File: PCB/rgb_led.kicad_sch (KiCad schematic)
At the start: 3 parts

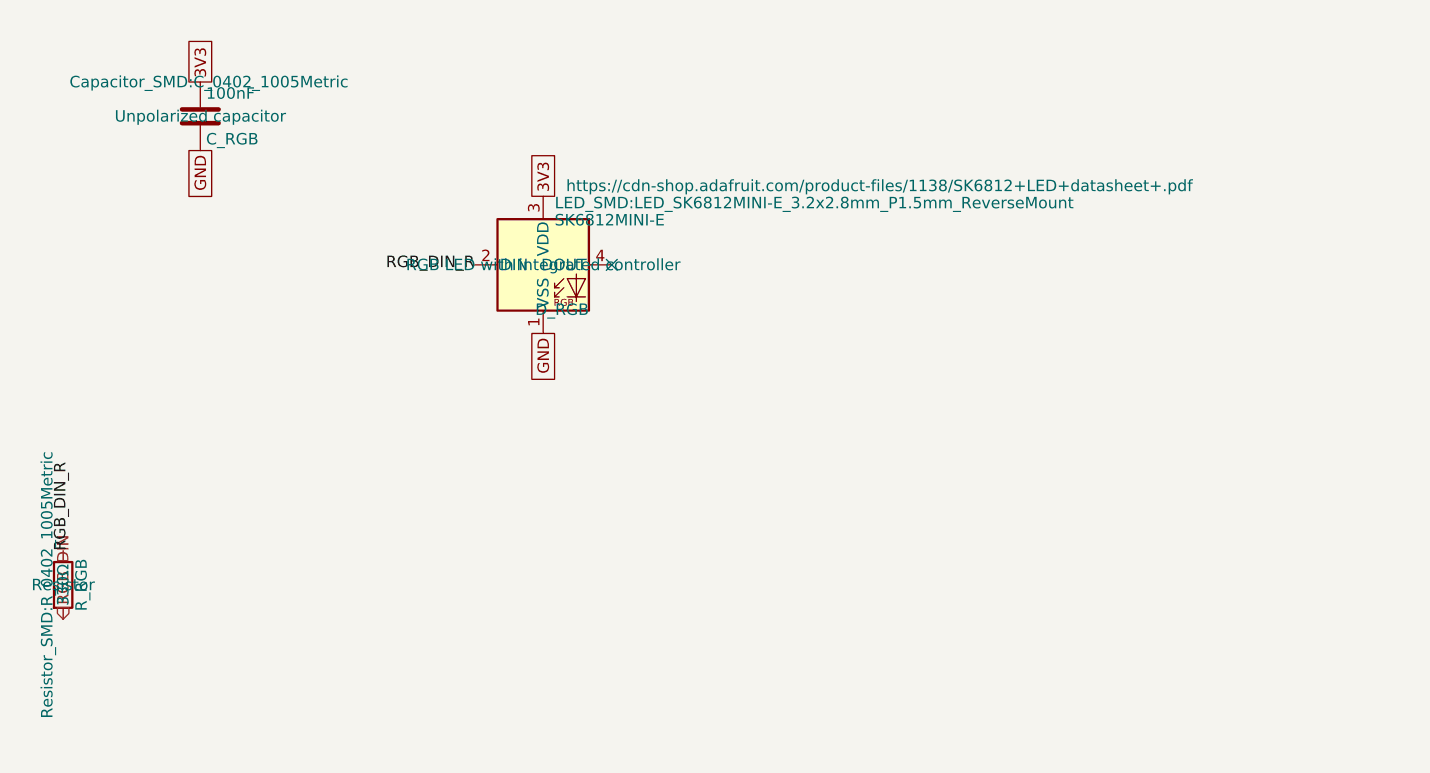
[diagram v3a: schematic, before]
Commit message: layout: everything is on the board
The board edge cuts are down to 100mm x 35mm. All the components have the right footprints and are on the board, but no traces exist yet, and not all circuits are laid out properly yet. Lots of DRC warnings.
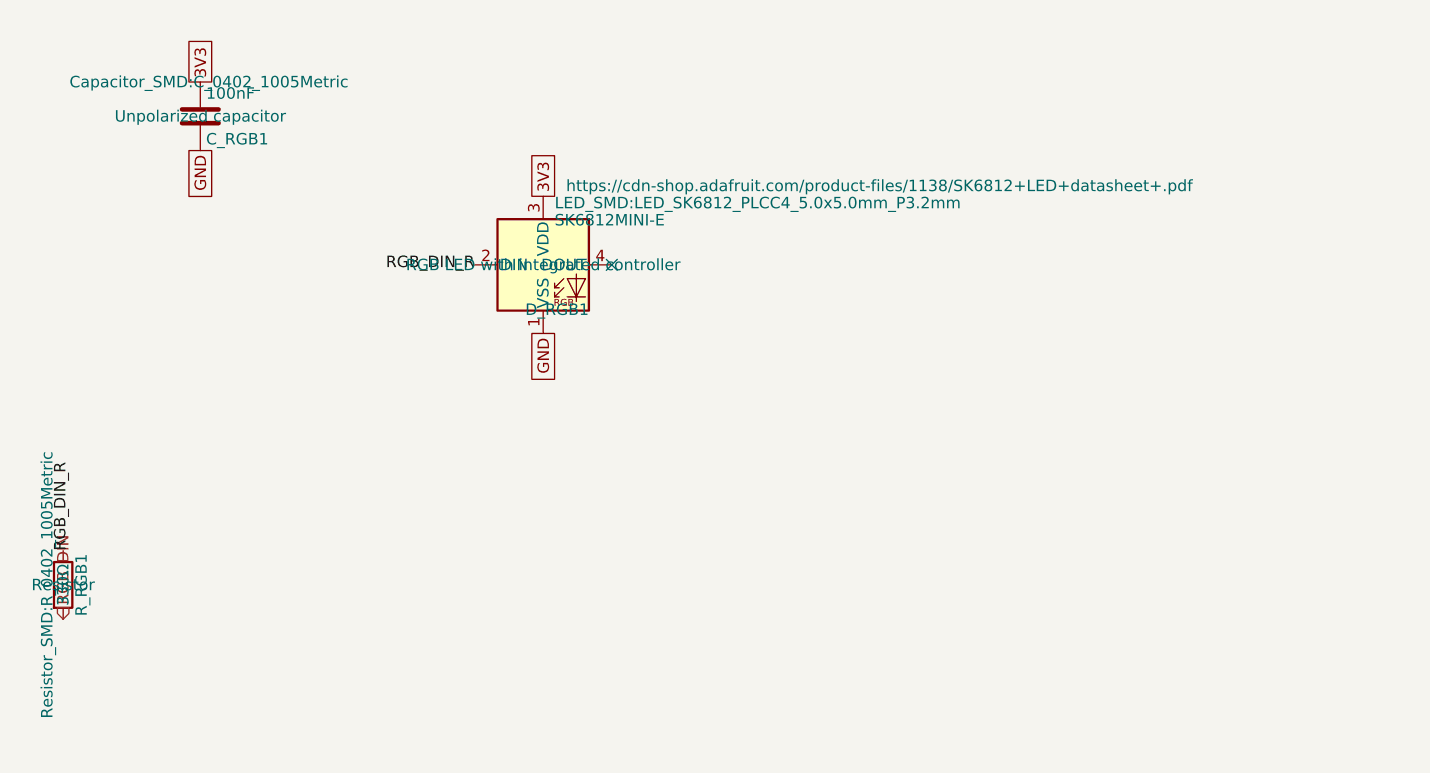
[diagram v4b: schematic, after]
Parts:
- removed C_RGB: 100nF, Capacitor_SMD:C_0402_1005Metric, symbol Device:C
- removed D_RGB: SK6812MINI-E, LED_SMD:LED_SK6812MINI-E_3.2x2.8mm_P1.5mm_ReverseMount, symbol LED:SK6812
- removed R_RGB: 330Ω, Resistor_SMD:R_0402_1005Metric, symbol Device:R
- added C_RGB1: 100nF, Capacitor_SMD:C_0402_1005Metric, symbol Device:C
- added D_RGB1: SK6812MINI-E, LED_SMD:LED_SK6812_PLCC4_5.0x5.0mm_P3.2mm, symbol LED:SK6812
- added R_RGB1: 330Ω, Resistor_SMD:R_0402_1005Metric, symbol Device:R
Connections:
- net 3V3: now also C_RGB1.1, D_RGB1.3 (VDD)
- net GND: now also C_RGB1.2, D_RGB1.1 (VSS)
- net RGB_DIN: now also R_RGB1.2
- net RGB_DIN_R: now also D_RGB1.2 (DIN), R_RGB1.1
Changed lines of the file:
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@@
+		)
+	)
+	(global_label "GND"
+		(shape passive)
+		(at 175.26 102.87 270)
+		(fields_autoplaced yes)
+		(effects
+			(font
+				(size 1.27 1.27)
+			)
+			(justify right)
+		)
+		(property "Intersheetrefs" "${INTERSHEET_REFS}"
+			(at 175.26 102.87 0)
+			(hide yes)
+			(show_name no)
+			(do_not_autoplace no)
+			(effects
+				(font
+					(size 1.27 1.27)
+				)
+			)
+		)
+	)
+	(global_label "GND"
+		(shape passive)
+		(at 137.16 82.55 270)
+		(fields_autoplaced yes)
+		(effects
+			(font
+				(size 1.27 1.27)
+			)
+			(justify right)
+		)
+		(property "Intersheetrefs" "${INTERSHEET_REFS}"
+			(at 137.16 82.55 0)
+			(hide yes)
+			(show_name no)
+			(do_not_autoplace no)
+			(effects
+				(font
+					(size 1.27 1.27)
+				)
+			)
+		)
+	)
+	(global_label "3V3"
+		(shape passive)
+		(at 137.16 74.93 90)
+		(fields_autoplaced yes)
+		(effects
+			(font
+				(size 1.27 1.27)
+			)
+			(justify left)
+		)
+		(property "Intersheetrefs" "${INTERSHEET_REFS}"
+			(at 137.16 74.93 0)
+			(hide yes)
+			(show_name no)
+			(do_not_autoplace no)
+			(effects
+				(font
+					(size 1.27 1.27)
+				)
+			)
 		)
 	)
@@
 		(property "Intersheetrefs" "${INTERSHEET_REFS}"
 			(at 175.26 87.63 0)
-			(hide yes)
-			(show_name no)
-			(do_not_autoplace no)
-			(effects
-				(font
-					(size 1.27 1.27)
-				)
-			)
-		)
-	)
-	(global_label "GND"
-		(shape passive)
-		(at 175.26 102.87 270)
-		(fields_autoplaced yes)
-		(effects
-			(font
-				(size 1.27 1.27)
-			)
-			(justify right)
-		)
-		(property "Intersheetrefs" "${INTERSHEET_REFS}"
-			(at 175.26 102.87 0)
-			(hide yes)
-			(show_name no)
-			(do_not_autoplace no)
-			(effects
-				(font
-					(size 1.27 1.27)
-				)
-			)
-		)
-	)
-	(global_label "GND"
-		(shape passive)
-		(at 137.16 82.55 270)
-		(fields_autoplaced yes)
-		(effects
-			(font
-				(size 1.27 1.27)
-			)
-			(justify right)
-		)
-		(property "Intersheetrefs" "${INTERSHEET_REFS}"
-			(at 137.16 82.55 0)
-			(hide yes)
-			(show_name no)
-			(do_not_autoplace no)
-			(effects
-				(font
-					(size 1.27 1.27)
-				)
-			)
-		)
-	)
-	(global_label "3V3"
-		(shape passive)
-		(at 137.16 74.93 90)
-		(fields_autoplaced yes)
-		(effects
-			(font
-				(size 1.27 1.27)
-			)
-			(justify left)
-		)
-		(property "Intersheetrefs" "${INTERSHEET_REFS}"
-			(at 137.16 74.93 0)
 			(hide yes)
 			(show_name no)
@@
 		(dnp no)
 		(fields_autoplaced yes)
-		(property "Reference" "C_RGB"
+		(property "Reference" "C_RGB1"
 			(at 137.795 81.28 0)
 			(show_name no)
@@
 		(instances
 			(project "snips_controller"
-				(path "/f9d779c6-e1a6-4677-9004-6e9cc3d2fa8d/de2e61c0-3a94-4f0a-93aa-fbb224e49852"
-					(reference "C_RGB")
+				(path "/21935953-32a0-46ad-8079-8177920c6978/b63260e5-0a73-448f-8e04-69b17654f975"
+					(reference "C_RGB1")
+					(unit 1)
+				)
+			)
+		)
+	)
+	(symbol
+		(lib_id "Device:R")
+		(at 121.92 130.81 0)
+		(unit 1)
+		(body_style 1)
+		(exclude_from_sim no)
+		(in_bom yes)
+		(on_board yes)
+		(in_pos_files yes)
+		(dnp no)
+		(fields_autoplaced yes)
+		(property "Reference" "R_RGB1"
+			(at 123.952 130.81 90)
+			(show_name no)
+			(do_not_autoplace no)
+			(effects
+				(font
+					(size 1.27 1.27)
+				)
+			)
+		)
+		(property "Value" "330Ω"
+			(at 121.92 130.81 90)
+			(show_name no)
+			(do_not_autoplace no)
+			(effects
+				(font
+					(size 1.27 1.27)
+				)
+			)
+		)
+		(property "Footprint" "Resistor_SMD:R_0402_1005Metric"
+			(at 120.142 130.81 90)
+			(show_name no)
+			(do_not_autoplace no)
+			(effects
+				(font
+					(size 1.27 1.27)
+				)
+			)
+		)
+		(property "Datasheet" ""
+			(at 121.92 130.81 0)
+			(show_name no)
+			(do_not_autoplace no)
+			(effects
+				(font
+					(size 1.27 1.27)
+				)
+			)
+		)
+		(property "Description" "Resistor"
+			(at 121.92 130.81 0)
+			(show_name no)
+			(do_not_autoplace no)
+			(effects
+				(font
+					(size 1.27 1.27)
+				)
+			)
+		)
+		(pin "1"
+		)
+		(pin "2"
+		)
+		(instances
+			(project "snips_controller"
+				(path "/21935953-32a0-46ad-8079-8177920c6978/b63260e5-0a73-448f-8e04-69b17654f975"
+					(reference "R_RGB1")
 					(unit 1)
 				)
@@
 		(dnp no)
 		(fields_autoplaced yes)
-		(property "Reference" "D_RGB"
+		(property "Reference" "D_RGB1"
 			(at 180.34 100.965 0)
 			(show_name no)
@@
 			)
 		)
-		(property "Footprint" "LED_SMD:LED_SK6812MINI-E_3.2x2.8mm_P1.5mm_ReverseMount"
+		(property "Footprint" "LED_SMD:LED_SK6812_PLCC4_5.0x5.0mm_P3.2mm"
 			(at 176.53 87.63 0)
 			(show_name no)
@@
 		(instances
 			(project "snips_controller"
-				(path "/f9d779c6-e1a6-4677-9004-6e9cc3d2fa8d/de2e61c0-3a94-4f0a-93aa-fbb224e49852"
-					(reference "D_RGB")
+				(path "/21935953-32a0-46ad-8079-8177920c6978/b63260e5-0a73-448f-8e04-69b17654f975"
+					(reference "D_RGB1")
 					(unit 1)
 				)
-			)
-		)
-	)
-	(symbol
-		(lib_id "Device:R")
-		(at 121.92 130.81 0)
-		(unit 1)
-		(body_style 1)
-		(exclude_from_sim no)
-		(in_bom yes)
-		(on_board yes)
-		(in_pos_files yes)
-		(dnp no)
-		(fields_autoplaced yes)
-		(property "Reference" "R_RGB"
-			(at 123.952 130.81 90)
-			(show_name no)
-			(do_not_autoplace no)
-			(effects
-				(font
-					(size 1.27 1.27)
-				)
-			)
-		)
-		(property "Value" "330Ω"
-			(at 121.92 130.81 90)
-			(show_name no)
-			(do_not_autoplace no)
-			(effects
-				(font
-					(size 1.27 1.27)
-				)
-			)
-		)
-		(property "Footprint" "Resistor_SMD:R_0402_1005Metric"
-			(at 120.142 130.81 90)
-			(show_name no)
-			(do_not_autoplace no)
-			(effects
-				(font
-					(size 1.27 1.27)
-				)
-			)
-		)
-		(property "Datasheet" ""
-			(at 121.92 130.81 0)
-			(show_name no)
-			(do_not_autoplace no)
-			(effects
-				(font
-					(size 1.27 1.27)
-				)
-			)
-		)
-		(property "Description" "Resistor"
-			(at 121.92 130.81 0)
-			(show_name no)
-			(do_not_autoplace no)
-			(effects
-				(font
-					(size 1.27 1.27)
-				)
-			)
-		)
-		(pin "1"
-		)
-		(pin "2"
-		)
-		(instances
-			(project "snips_controller"
-				(path "/f9d779c6-e1a6-4677-9004-6e9cc3d2fa8d/de2e61c0-3a94-4f0a-93aa-fbb224e49852"
-					(reference "R_RGB")
-					(unit 1)
-				)

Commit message: task: part number populated (#26)
kicad-happy run part 2 - MPN numbers populated
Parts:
- C_RGB1: MF (none) -> Yageo; Manufacturer_Part_Number (none) -> CC0402KRX7R9BB104
- D_RGB1: MF (none) -> OPSCO Optoelectronics; Manufacturer_Part_Number (none) -> SK6812MINI-E
- R_RGB1: MF (none) -> Yageo; Manufacturer_Part_Number (none) -> RC0402FR-07330RL
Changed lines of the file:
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@@
+			)
+		)
+		(property "MF" "Yageo" (at 0 0 0)
+			(effects
+				(font
+					(size 1.27 1.27)
+				)
+				(hide yes)
+			)
+		)
+		(property "Manufacturer_Part_Number" "CC0402KRX7R9BB104" (at 0 0 0)
+			(effects
+				(font
+					(size 1.27 1.27)
+				)
+				(hide yes)
 			)
 		)
@@
 			)
 		)
+		(property "MF" "Yageo" (at 0 0 0)
+			(effects
+				(font
+					(size 1.27 1.27)
+				)
+				(hide yes)
+			)
+		)
+		(property "Manufacturer_Part_Number" "RC0402FR-07330RL" (at 0 0 0)
+			(effects
+				(font
+					(size 1.27 1.27)
+				)
+				(hide yes)
+			)
+		)
 		(pin "1"
 		)
@@
 			)
 		)
+		(property "MF" "OPSCO Optoelectronics" (at 0 0 0)
+			(effects
+				(font
+					(size 1.27 1.27)
+				)
+				(hide yes)
+			)
+		)
+		(property "Manufacturer_Part_Number" "SK6812MINI-E" (at 0 0 0)
+			(effects
+				(font
+					(size 1.27 1.27)
+				)
+				(hide yes)
+			)
+		)
